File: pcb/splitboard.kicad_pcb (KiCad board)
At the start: 2 copper layers, 222.9 x 95.2 mm, 150 parts, among them IC1 ATMEGA32U4-MU, J1 Conn_02x05_Counter_Clockwise, J2 Conn_droite, J3 Conn_On_Off, Q1 Q_NPN_BCE, Q2 Q_NPN_BCE, SW1 SW_Push_LED, SW10 SW_Push_LED, SW101 SPST_TACT-KMR2, SW11 SW_Push_LED, SW12 SW_Push_LED, SW13 SW_Push_LED, SW14 SW_Push_LED, SW15 SW_Push_LED, SW16 SW_Push_LED, SW17 SW_Push_LED, SW18 SW_Push_LED, SW19 SW_Push_LED, SW2 SW_Push_LED, SW20 SW_Push_LED, SW21 SW_Push_LED, SW22 SW_Push_LED, SW23 SW_Push_LED, SW24 SW_Push_LED, SW25 SW_Push_LED, SW26 SW_Push_LED, SW27 SW_Push_LED, SW28 SW_Push_LED, SW29 SW_Push_LED, SW3 SW_Push_LED, SW30 SW_Push_LED, SW31 SW_Push_LED, SW32 SW_Push_LED, SW33 SW_Push_LED, SW34 SW_Push_LED, SW35 SW_Push_LED, SW36 SW_Push_LED, SW37 SW_Push_LED, SW38 SW_Push_LED, SW39 SW_Push_LED, SW40 SW_Push_LED, SW41 SW_Push_LED, SW42 SW_Push_LED, SW43 SW_Push_LED, SW44 SW_Push_LED, SW45 SW_Push_LED, SW46 SW_Push_LED, SW47 SW_Push_LED, SW5 SW_Push_LED, SW50 Rotary_Encoder, SW6 SW_Push_LED, SW7 SW_Push_LED, SW8 SW_Push_LED, SW9 SW_Push_LED, U1 TCA9555DBR, U2 TCA9555DBR, U3 MCP73831T-2ACI/OT, U4 SPX3819-3.3, U5 MBT40, X3 microUSB, Y1 8MHz

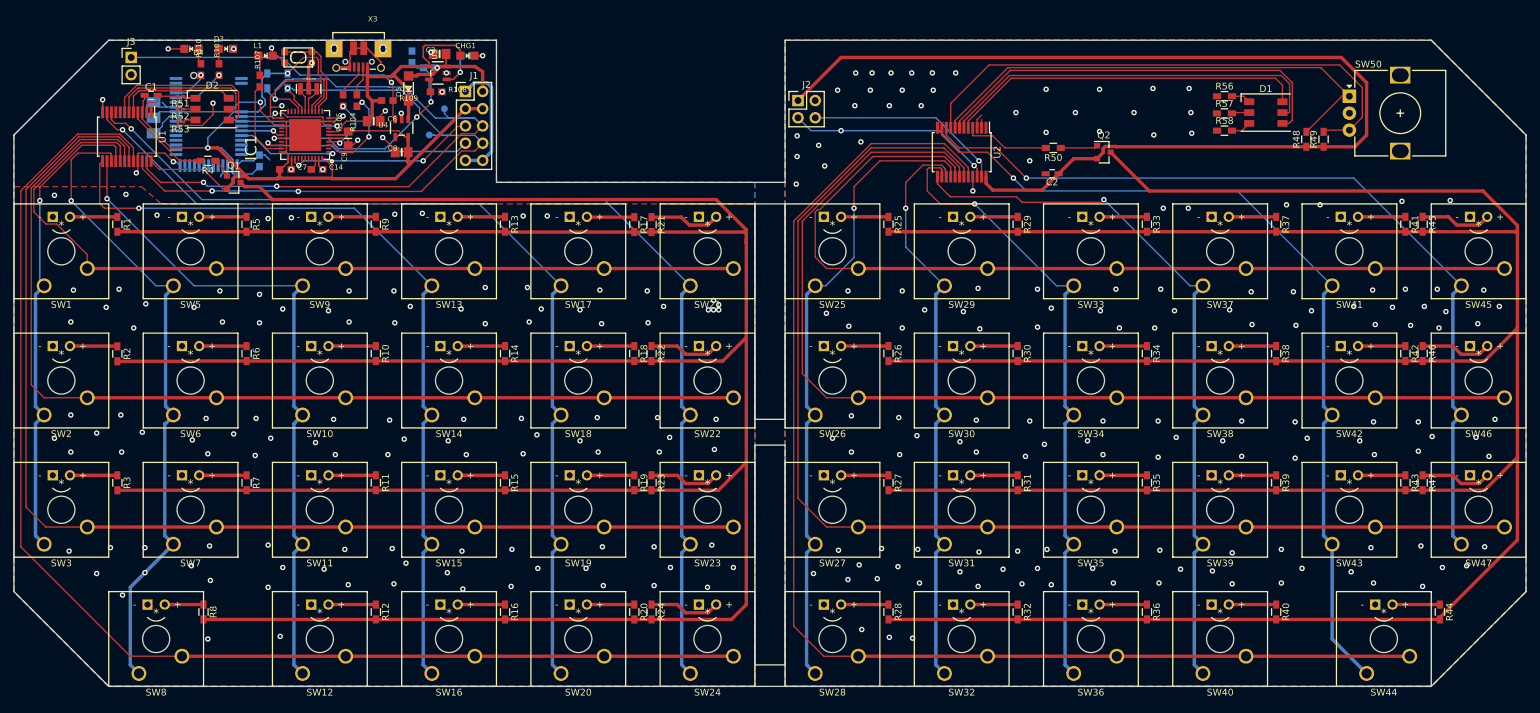
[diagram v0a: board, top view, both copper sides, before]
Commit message: added hole for screws in kicad
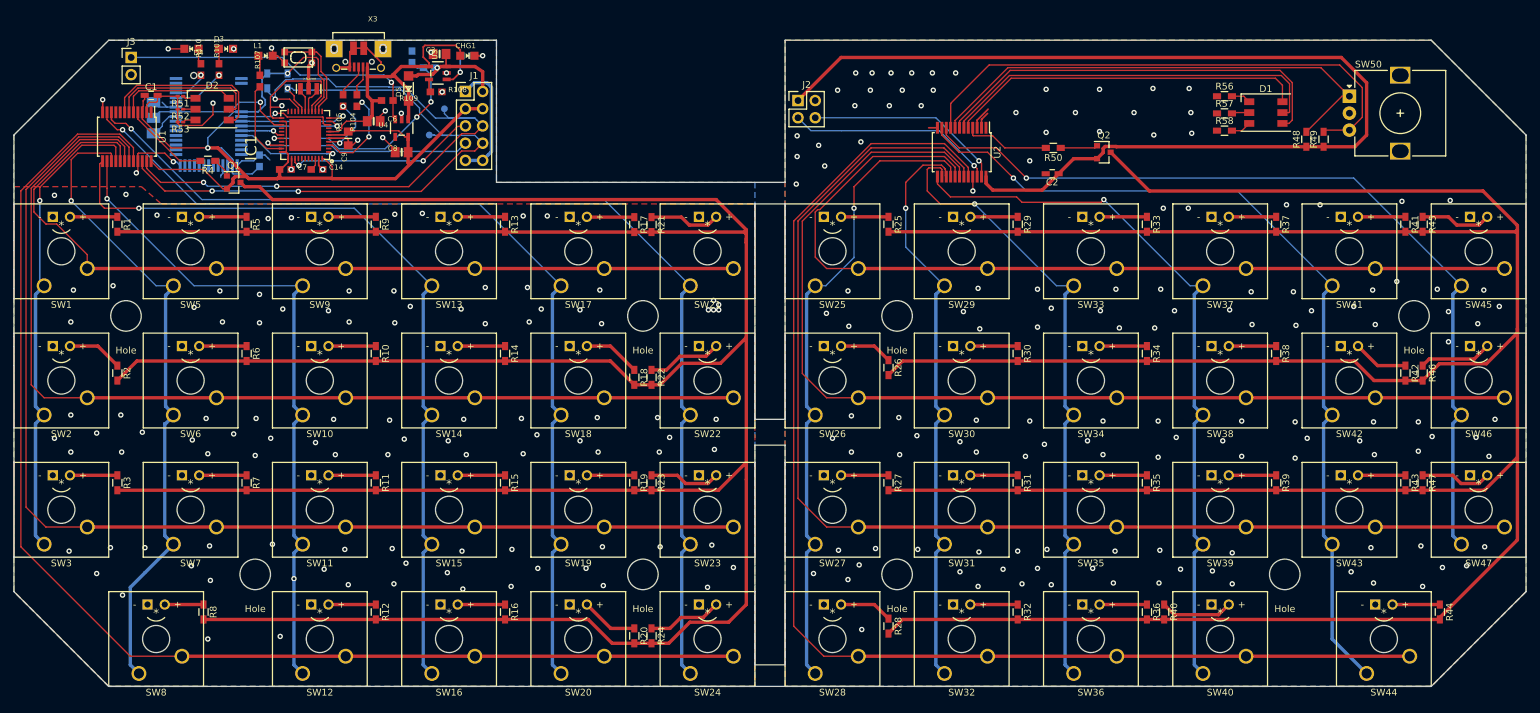
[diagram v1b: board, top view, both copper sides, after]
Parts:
- added Hole: screw hole, splitboard:screw hole, F.Cu at (222.9, 100.3)
- added Hole: screw hole, splitboard:screw hole, F.Cu at (203.8, 138.4)
- added Hole: screw hole, splitboard:screw hole, F.Cu at (146.7, 100.3)
- added Hole: screw hole, splitboard:screw hole, F.Cu at (146.7, 138.4)
- added Hole: screw hole, splitboard:screw hole, F.Cu at (109.2, 138.4)
- added Hole: screw hole, splitboard:screw hole, F.Cu at (52.1, 138.4)
- added Hole: screw hole, splitboard:screw hole, F.Cu at (33.0, 100.3)
- added Hole: screw hole, splitboard:screw hole, F.Cu at (109.2, 100.3)
- moved R40 16.5 mm to (186.1, 144.0)
- moved R20 3.52 mm to (108.0, 147.5)
- moved R24 3.52 mm to (110.5, 147.5)
- moved R18 3.52 mm to (108.0, 109.4)
- moved R22 3.52 mm to (110.5, 109.4)
- moved R42 2.88 mm to (221.6, 108.8)
- moved R46 2.88 mm to (224.2, 108.8)
- moved R2 2.84 mm to (31.8, 108.8)
- moved R28 2.08 mm to (145.4, 146.1)
- moved R26 2.08 mm to (145.4, 108.0)
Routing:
- net Net-(Q1-Pad3): track 495.7 -> 502.7 mm
- net Net-(Q2-Pad3): track 490.4 -> 494.8 mm
- net gnd1: track 5.48 -> 9.33 mm, vias 150 -> 136
- net Net-(R40-Pad1): track 6.98 -> 10.8 mm
- net Net-(R18-Pad1): track 6.98 -> 8.44 mm
- net Net-(R20-Pad1): track 6.98 -> 8.44 mm
- net Net-(R42-Pad1): track 6.99 -> 8.18 mm
- net Net-(R2-Pad1): track 7.00 -> 8.18 mm
- net Net-(R28-Pad1): track 6.98 -> 7.84 mm
- net Net-(R26-Pad1): track 6.98 -> 7.84 mm
- net Net-(U2-Pad1): track 0.00 -> 0.61 mm
- net scl1: vias 2 -> 1
- net Net-(SW5-Pad1): vias 2 -> 1
- net Net-(SW10-Pad1): vias 1 -> 2
- net GND: vias 130 -> 120

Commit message: holes dimensions
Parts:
- removed the Hole at (222.9, 100.3)
- removed the Hole at (203.8, 138.4)
- removed the Hole at (146.7, 100.3)
- removed the Hole at (146.7, 138.4)
- removed the Hole at (109.2, 138.4)
- removed the Hole at (52.1, 138.4)
- removed the Hole at (33.0, 100.3)
- added Hole: M3, splitboard:screwhole, F.Cu at (222.9, 100.3)
- added Hole: M3, splitboard:screwhole, F.Cu at (203.8, 138.4)
- added Hole: M3, splitboard:screwhole, F.Cu at (146.7, 100.3)
- added Hole: M3, splitboard:screwhole, F.Cu at (146.7, 138.4)
- added Hole: M3, splitboard:screwhole, F.Cu at (109.2, 138.4)
- added Hole: M3, splitboard:screwhole, F.Cu at (52.1, 138.4)
- added Hole: M3, splitboard:screwhole, F.Cu at (33.0, 100.3)
- Hole: value screw hole -> M3; footprint splitboard:screw hole -> splitboard:screwhole

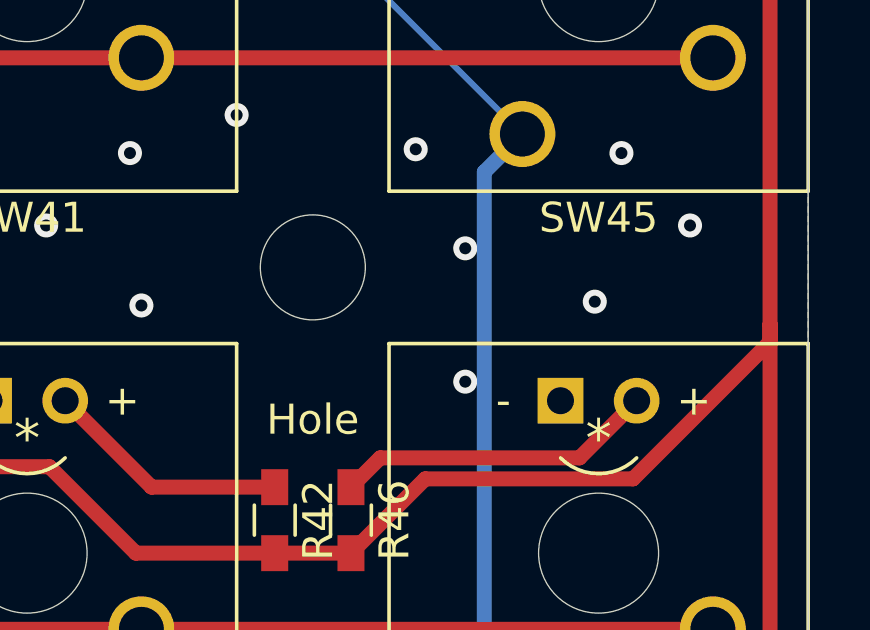
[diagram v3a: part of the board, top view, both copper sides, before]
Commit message: pcb via
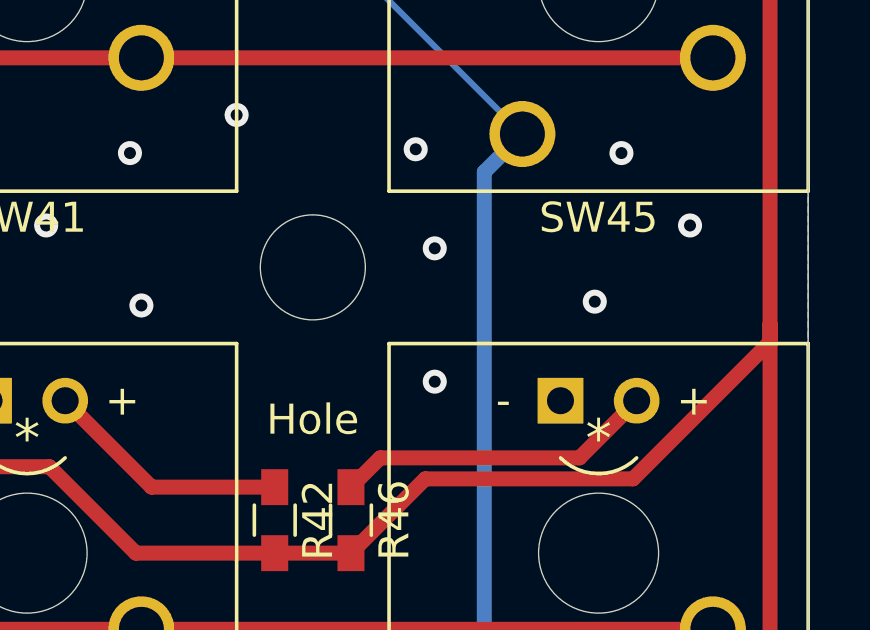
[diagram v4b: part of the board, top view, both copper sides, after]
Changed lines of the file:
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@@
     (0 F.Cu signal)
     (31 B.Cu signal)
-    (32 B.Adhes user)
+    (32 B.Adhes user hide)
     (33 F.Adhes user hide)
     (34 B.Paste user)
@@
   (via (at 220.345 95.25) (size 0.8) (drill 0.4) (layers F.Cu B.Cu) (net 4))
   (via (at 226.314 96.393) (size 0.8) (drill 0.4) (layers F.Cu B.Cu) (net 4))
-  (via (at 227.965 99.695) (size 0.8) (drill 0.4) (layers F.Cu B.Cu) (net 4))
-  (via (at 227.965 104.14) (size 0.8) (drill 0.4) (layers F.Cu B.Cu) (net 4))
+  (via (at 226.949 99.695) (size 0.8) (drill 0.4) (layers F.Cu B.Cu) (net 4))
+  (via (at 226.949 104.14) (size 0.8) (drill 0.4) (layers F.Cu B.Cu) (net 4))
   (via (at 217.17 101.6) (size 0.8) (drill 0.4) (layers F.Cu B.Cu) (net 4))
   (via (at 233.172 96.52) (size 0.8) (drill 0.4) (layers F.Cu B.Cu) (net 4))
